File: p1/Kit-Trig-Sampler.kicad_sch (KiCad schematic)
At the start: 78 parts, among them J1 START_CV, J10 AUDIO_INR, J11 AUDIO_OUTL, J12 Eurorack_Power_16pin_Unshroud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, J2 LENGTH_CV, J3 SAMP_CV, J4 PITCH CV, J5 REV_TRIG, J6 PLAY_TRIG, J7 END_OUT, J8 AUDIO_INL, J9 AUIDO_OUTR, U1 TL082_TH, U2 TL082_TH

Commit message: Small changes to pin assignments
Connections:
- net A1: now also C1.1, POT_PITCH1.2 (Center); no longer R3.2, R6.2
- net A3: now also C10.1, POT_START1.2 (Center); no longer R4.2, R7.2
- net A4: no longer C1.1, POT_PITCH1.2 (Center)
- net A5: now also R3.2, R6.2; no longer C2.1, POT_SAMP1.2 (Center)
- net A6: now also C18.1, R27.2; no longer C10.1, POT_START1.2 (Center)
- net A8: now also R4.2, R7.2
- net A9: now also C2.1, POT_SAMP1.2 (Center); no longer C18.1, R27.2
- net D10: no longer R20.1
- net D11: now also R18.1; no longer R24.2
- net D12: now also R19.1; no longer R21.1
- net D15: now also R12.1; no longer J5.1 (SIG)
- net D16: now also R32.2, SD1.8 (DAT1); no longer R31.2, SD1.7 (DAT0)
- net D17: now also R31.2, SD1.7 (DAT0); no longer R32.2, SD1.8 (DAT1)
- net D18: now also R30.2, SD1.3 (CMD); no longer R28.2, SD1.1 (DAT2)
- net D19: now also R28.2, SD1.1 (DAT2); no longer R30.2, SD1.3 (CMD)
- net D2: now also J5.1 (SIG); no longer R12.1
- net D3: now also R24.2; no longer R19.1
- net D5: now also R20.1
- net D7: now also R21.1; no longer R18.1
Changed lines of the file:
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@@
     (effects (font (size 1.27 1.27)) (justify left bottom))
   )
-  (text "Length_CV" (at 471.17 262.255 0)
-    (effects (font (size 1.27 1.27)) (justify left bottom))
-  )
-  (text "Rev_Trig" (at 387.985 267.335 0)
+  (text "Length_CV" (at 471.17 267.335 0)
+    (effects (font (size 1.27 1.27)) (justify left bottom))
+  )
+  (text "Rev_Trig" (at 387.985 272.415 0)
     (effects (font (size 1.27 1.27)) (justify left bottom))
   )
@@
     (effects (font (size 5.08 5.08) (thickness 1.016) bold italic) (justify left bottom))
   )
-  (text "Play_But_R" (at 327.66 272.415 0)
-    (effects (font (size 1.27 1.27)) (justify left bottom))
-  )
-  (text "Rev_But_G" (at 313.69 133.985 0)
+  (text "Play_But_R" (at 387.985 234.315 0)
+    (effects (font (size 1.27 1.27)) (justify left bottom))
+  )
+  (text "Rev_But_G" (at 366.395 143.51 0)
     (effects (font (size 1.27 1.27)) (justify left bottom))
   )
@@
     (effects (font (size 1.27 1.27)) (justify left bottom))
   )
-  (text "Start_Pot" (at 433.705 269.875 0)
+  (text "Start_Pot" (at 471.17 264.795 0)
     (effects (font (size 1.27 1.27)) (justify left bottom))
   )
@@
     (effects (font (size 1.27 1.27)) (justify left bottom))
   )
-  (text "SDMMC_D2" (at 497.84 88.9 180)
-    (effects (font (size 1.27 1.27)) (justify right bottom))
-  )
-  (text "SDMMC_D0" (at 497.84 73.66 180)
-    (effects (font (size 1.27 1.27)) (justify right bottom))
-  )
-  (text "Length_Pot" (at 471.17 269.875 0)
+  (text "SDMMC_D2" (at 497.84 83.82 180)
+    (effects (font (size 1.27 1.27)) (justify right bottom))
+  )
+  (text "SDMMC_D0" (at 497.84 71.12 180)
+    (effects (font (size 1.27 1.27)) (justify right bottom))
+  )
+  (text "Length_Pot" (at 471.805 269.875 0)
     (effects (font (size 1.27 1.27)) (justify left bottom))
   )
@@
     (effects (font (size 5.08 5.08) (thickness 1.016) bold italic) (justify left bottom))
   )
-  (text "Rev_But" (at 471.17 272.415 0)
+  (text "Rev_But" (at 434.34 269.875 0)
     (effects (font (size 1.27 1.27)) (justify left bottom))
   )
@@
     (effects (font (size 1.27 1.27)) (justify left bottom))
   )
-  (text "SDMMC_D1" (at 497.84 71.12 180)
+  (text "SDMMC_D1" (at 497.84 73.66 180)
     (effects (font (size 1.27 1.27)) (justify right bottom))
   )
@@
     (effects (font (size 5.08 5.08) (thickness 1.016) bold italic) (justify left bottom))
   )
-  (text "Pitch_Pot" (at 433.07 267.335 0)
-    (effects (font (size 1.27 1.27)) (justify left bottom))
-  )
-  (text "Bank_But_G" (at 416.56 230.505 0)
-    (effects (font (size 1.27 1.27)) (justify left bottom))
-  )
-  (text "Sample_Pot" (at 471.17 267.335 0)
+  (text "Pitch_Pot" (at 471.17 262.255 0)
+    (effects (font (size 1.27 1.27)) (justify left bottom))
+  )
+  (text "Bank_But_G" (at 328.295 272.415 0)
+    (effects (font (size 1.27 1.27)) (justify left bottom))
+  )
+  (text "Sample_Pot" (at 471.17 272.415 0)
     (effects (font (size 1.27 1.27)) (justify left bottom))
   )
@@
     (effects (font (size 1.27 1.27)) (justify left bottom))
   )
-  (text "Rev_But_G" (at 387.985 231.775 0)
+  (text "Rev_But_G" (at 387.35 231.775 0)
     (effects (font (size 1.27 1.27)) (justify left bottom))
   )
@@
     (effects (font (size 1.27 1.27)) (justify right bottom))
   )
-  (text "Play_But_G" (at 484.505 234.95 0)
+  (text "Play_But_G" (at 332.105 231.775 0)
     (effects (font (size 1.27 1.27)) (justify left bottom))
   )
@@
     (effects (font (size 1.27 1.27)) (justify right bottom))
   )
-  (text "Rev_But_R" (at 388.62 234.315 0)
+  (text "Rev_But_R" (at 484.505 235.585 0)
     (effects (font (size 1.27 1.27)) (justify left bottom))
   )
@@
     (effects (font (size 1.27 1.27)) (justify left bottom))
   )
-  (text "End_Out" (at 396.24 272.415 180)
+  (text "End_Out" (at 395.605 267.335 180)
     (effects (font (size 1.27 1.27)) (justify right bottom))
   )
@@
     (effects (font (size 1.27 1.27)) (justify left bottom))
   )
-  (text "SDMMC_D3" (at 497.84 83.82 180)
+  (text "SDMMC_D3" (at 497.84 88.9 180)
     (effects (font (size 1.27 1.27)) (justify right bottom))
   )
@@
     (effects (font (size 1.27 1.27)) (justify right bottom))
   )
-  (text "Rev_But_B" (at 367.665 144.145 0)
-    (effects (font (size 1.27 1.27)) (justify left bottom))
-  )
-  (text "Rev_But_B" (at 340.995 231.14 180)
+  (text "Rev_But_B" (at 311.785 133.35 0)
+    (effects (font (size 1.27 1.27)) (justify left bottom))
+  )
+  (text "Rev_But_B" (at 427.99 230.505 180)
     (effects (font (size 1.27 1.27)) (justify right bottom))
   )
@@
     (effects (font (size 1.27 1.27)) (justify left bottom))
   )
-  (text "Sample_CV" (at 471.17 264.795 0)
+  (text "Sample_CV" (at 431.165 272.415 0)
     (effects (font (size 1.27 1.27)) (justify left bottom))
   )
@@
     (effects (font (size 1.27 1.27)) (justify left bottom))
   )
-  (label "D7" (at 321.945 100.33 0)
+  (label "D11" (at 321.945 100.33 0)
     (effects (font (size 1.27 1.27)) (justify left bottom))
   )
@@
     (effects (font (size 1.27 1.27)) (justify right bottom))
   )
-  (label "A4" (at 52.07 239.395 180)
+  (label "A1" (at 52.07 239.395 180)
     (effects (font (size 1.27 1.27)) (justify right bottom))
   )
@@
     (effects (font (size 1.27 1.27)) (justify left bottom))
   )
-  (label "D11" (at 372.745 140.97 180)
+  (label "D3" (at 372.745 140.97 180)
     (effects (font (size 1.27 1.27)) (justify right bottom))
   )
@@
     (effects (font (size 1.27 1.27)) (justify right bottom))
   )
-  (label "D2" (at 152.4 115.57 0)
+  (label "D15" (at 152.4 115.57 0)
     (effects (font (size 1.27 1.27)) (justify left bottom))
   )
@@
     (effects (font (size 1.27 1.27)) (justify right bottom))
   )
-  (label "D18" (at 482.6 88.9 0)
-    (effects (font (size 1.27 1.27)) (justify left bottom))
-  )
-  (label "D16" (at 482.6 73.66 0)
+  (label "D18" (at 482.6 83.82 0)
+    (effects (font (size 1.27 1.27)) (justify left bottom))
+  )
+  (label "D16" (at 482.6 71.12 0)
     (effects (font (size 1.27 1.27)) (justify left bottom))
   )
@@
     (effects (font (size 1.27 1.27)) (justify right bottom))
   )
-  (label "A6" (at 111.125 271.78 180)
+  (label "A3" (at 111.125 271.78 180)
     (effects (font (size 1.27 1.27)) (justify right bottom))
   )
@@
     (effects (font (size 1.27 1.27)) (justify right bottom))
   )
-  (label "A5" (at 52.705 271.78 180)
-    (effects (font (size 1.27 1.27)) (justify right bottom))
-  )
-  (label "D15" (at 171.45 49.53 180)
+  (label "A9" (at 52.705 271.78 180)
+    (effects (font (size 1.27 1.27)) (justify right bottom))
+  )
+  (label "D2" (at 171.45 49.53 180)
     (effects (font (size 1.27 1.27)) (justify right bottom))
   )
@@
     (effects (font (size 1.27 1.27)) (justify right bottom))
   )
-  (label "D19" (at 482.6 83.82 0)
-    (effects (font (size 1.27 1.27)) (justify left bottom))
-  )
-  (label "A9" (at 374.015 125.73 180)
+  (label "D19" (at 482.6 88.9 0)
+    (effects (font (size 1.27 1.27)) (justify left bottom))
+  )
+  (label "A6" (at 374.015 125.73 180)
     (effects (font (size 1.27 1.27)) (justify right bottom))
   )
@@
     (effects (font (size 1.27 1.27)) (justify left bottom))
   )
-  (label "D12" (at 321.945 140.97 0)
+  (label "D7" (at 321.945 140.97 0)
     (effects (font (size 1.27 1.27)) (justify left bottom))
   )
@@
     (effects (font (size 1.27 1.27)) (justify right bottom))
   )
-  (label "A3" (at 73.025 127.635 180)
-    (effects (font (size 1.27 1.27)) (justify right bottom))
-  )
-  (label "D3" (at 321.945 105.41 0)
+  (label "A8" (at 73.025 127.635 180)
+    (effects (font (size 1.27 1.27)) (justify right bottom))
+  )
+  (label "D12" (at 321.945 105.41 0)
     (effects (font (size 1.27 1.27)) (justify left bottom))
   )
@@
     (effects (font (size 1.27 1.27)) (justify right bottom))
   )
-  (label "D17" (at 482.6 71.12 0)
+  (label "D17" (at 482.6 73.66 0)
     (effects (font (size 1.27 1.27)) (justify left bottom))
   )
@@
     (effects (font (size 1.27 1.27)) (justify left bottom))
   )
-  (label "D10" (at 321.945 135.89 0)
-    (effects (font (size 1.27 1.27)) (justify left bottom))
-  )
-  (label "A1" (at 72.39 86.36 180)
-    (effects (font (size 1.27 1.27)) (justify right bottom))
-  )
+  (label "D5" (at 321.945 135.89 0)
+    (effects (font (size 1.27 1.27)) (justify left bottom))
+  )
+  (label "A5" (at 72.39 86.36 180)
+    (effects (font (size 1.27 1.27)) (justify right bottom))
+  )

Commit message: added Bank cv
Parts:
- added J13: BANK_CV, 4ms_Jack:EighthInch_PJ398SM, symbol 4ms_Jack:3.5mm_Mono_Switched
- added R33: 47k_TH0.125, 4ms_Resistor:R_Axial_DIN0207_L6.3mm_D2.5mm_P7.62mm_Horizontal, symbol 4ms_Resistor_TH:47k_TH0.125
- added R34: 100k_TH0.125, 4ms_Resistor:R_Axial_DIN0207_L6.3mm_D2.5mm_P7.62mm_Horizontal, symbol 4ms_Resistor_TH:100k_TH0.125
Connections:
- net A4: now also R33.2, R34.2
- net GND: now also J13.2 (SHEILD), J13.3 (SW), R34.1
- new net: J13.1 (SIG), R33.1
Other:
- note added: "BANK_CV"
- moved on the sheet: C1, C10, C2, C3, C6, C9, J10, J11, J4, J8, J9, POT_LENGTH1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

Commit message: part placement ip
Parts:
- renumbered J12 to J14
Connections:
- net D10: now also R24.2
- net D3: no longer R24.2
- net at C11.2, R14.2, R15.1: now also U2.1; no longer U2.7
- net at C11.1, R13.2, R14.1: now also U2.2 (-); no longer U2.6 (-)
- net at R12.2: now also U2.3 (+); no longer U2.5 (+)
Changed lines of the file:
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@@
     (effects (font (size 1.27 1.27)) (justify left bottom))
   )
-  (label "D3" (at 372.745 140.97 180)
+  (label "D10" (at 372.745 140.97 180)
     (effects (font (size 1.27 1.27)) (justify right bottom))
   )
@@
   (symbol (lib_id "4ms_Connector:Eurorack_Power_16pin_Unshrouded") (at 38.735 369.57 0) (unit 1)
     (in_bom yes) (on_board yes) (fields_autoplaced)
-    (property "Reference" "J12" (id 0) (at 36.6363 383.54 0))
+    (property "Reference" "J14" (id 0) (at 36.6363 383.54 0))
     (property "Value" "Eurorack_Power_16pin_Unshrouded" (id 1) (at 36.6363 386.08 0))
     (property "Footprint" "4ms_Connector:Pins_2x08_2.54mm_TH_EuroPower" (id 2) (at 48.895 392.43 0)
@@
     (pin "1")
   )
-  (symbol (lib_id "4ms_IC:TL082_TH") (at 191.77 118.11 0) (unit 2)
+  (symbol (lib_id "4ms_IC:TL082_TH") (at 191.77 118.11 0) (unit 1)
     (in_bom yes) (on_board yes) (fields_autoplaced)
     (property "Reference" "U2" (id 0) (at 191.77 107.95 0))
@@
       (reference "J11") (unit 1) (value "AUDIO_OUTL") (footprint "4ms_Jack:EighthInch_PJ398SM")
     )
-    (path "/26de500a-6a5a-4f52-a622-63f695723fe5"
-      (reference "J12") (unit 1) (value "Eurorack_Power_16pin_Unshrouded") (footprint "4ms_Connector:Pins_2x08_2.54mm_TH_EuroPower")
-    )
     (path "/8dfd5b71-d7ca-434d-99e0-1511a2784fa0"
       (reference "J13") (unit 1) (value "BANK_CV") (footprint "4ms_Jack:EighthInch_PJ398SM")
     )
+    (path "/26de500a-6a5a-4f52-a622-63f695723fe5"
+      (reference "J14") (unit 1) (value "Eurorack_Power_16pin_Unshrouded") (footprint "4ms_Connector:Pins_2x08_2.54mm_TH_EuroPower")
+    )
     (path "/aa429c81-7bec-4d11-98d8-90f9522e0b59"
       (reference "JA1") (unit 1) (value "Socket_02x05_TH") (footprint "4ms_Connector:Socket_2x05_2.54mm_TH")
@@
     )
     (path "/e9d45a74-69c4-44b2-aeb2-b4cba2a5826a"
-      (reference "U2") (unit 2) (value "TL082_TH") (footprint "4ms_Package_DIP:DIP-8pin_TH")
+      (reference "U2") (unit 1) (value "TL082_TH") (footprint "4ms_Package_DIP:DIP-8pin_TH")
     )
     (path "/867c8e1f-3163-4dae-bd9c-3cfb52f58b42"

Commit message: small updates
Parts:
- Bank_But1: renamed from BANK_BUT1; footprint 4ms_Switch:Button_RgbLED_SPST_PB615303HL-7mm -> 4ms_Switch:Button_RgbLED_SPST_TC002
- REV_BUT1: footprint 4ms_Switch:Button_RgbLED_SPST_PB615303HL-7mm -> 4ms_Switch:Button_RgbLED_SPST_TC002
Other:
- moved on the sheet: J10, J8, J9

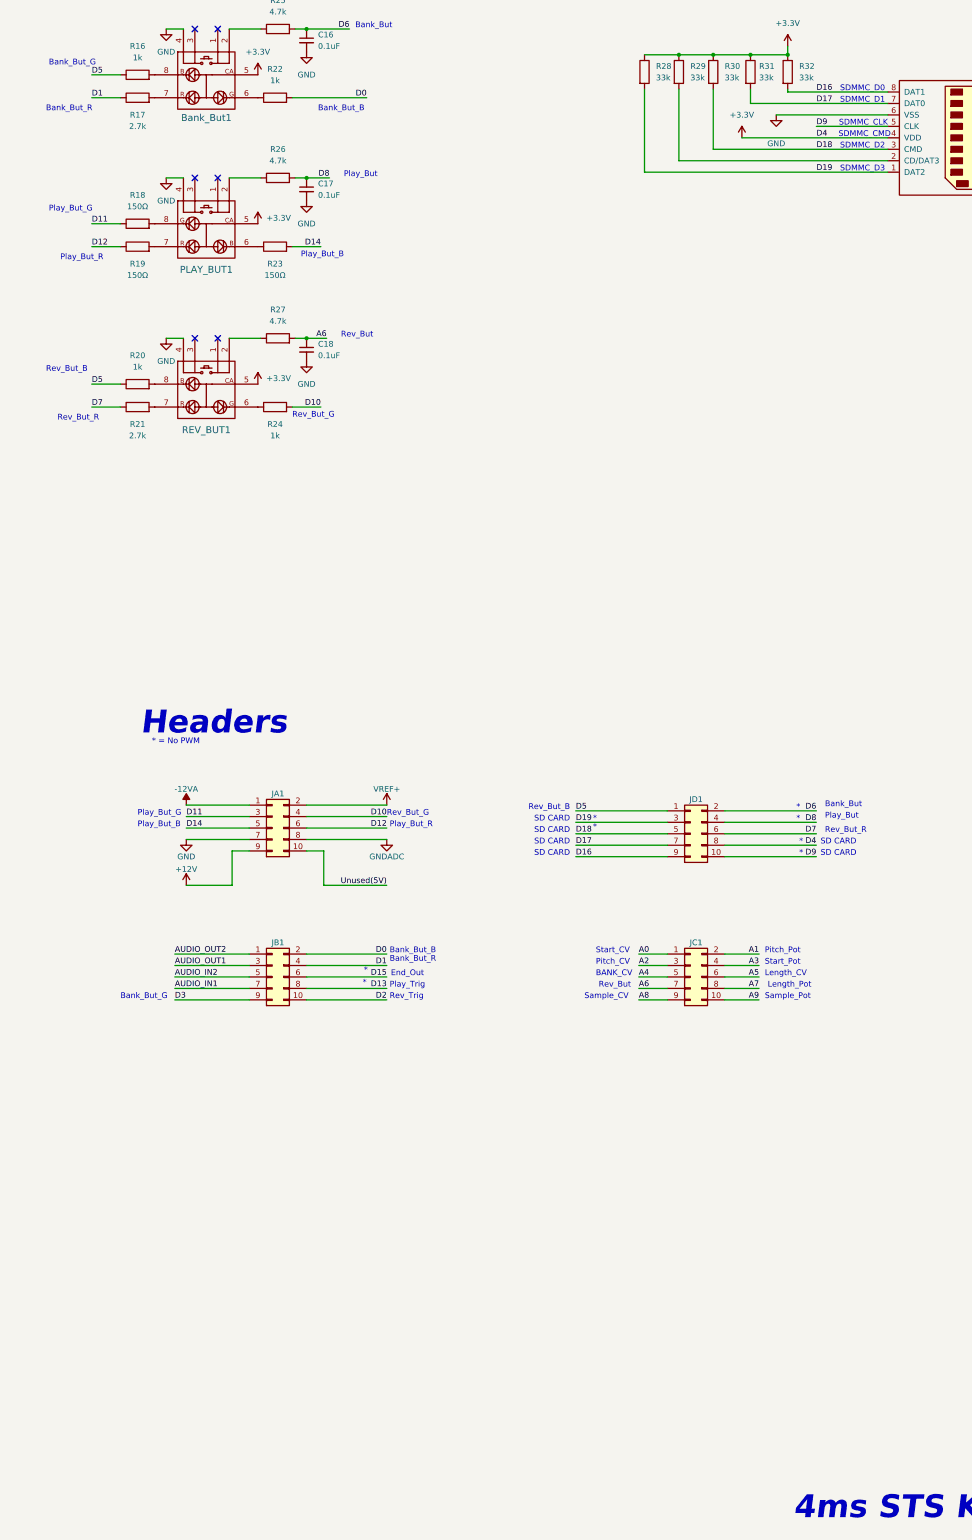
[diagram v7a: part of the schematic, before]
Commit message: nudged some parts in accordance to FP update
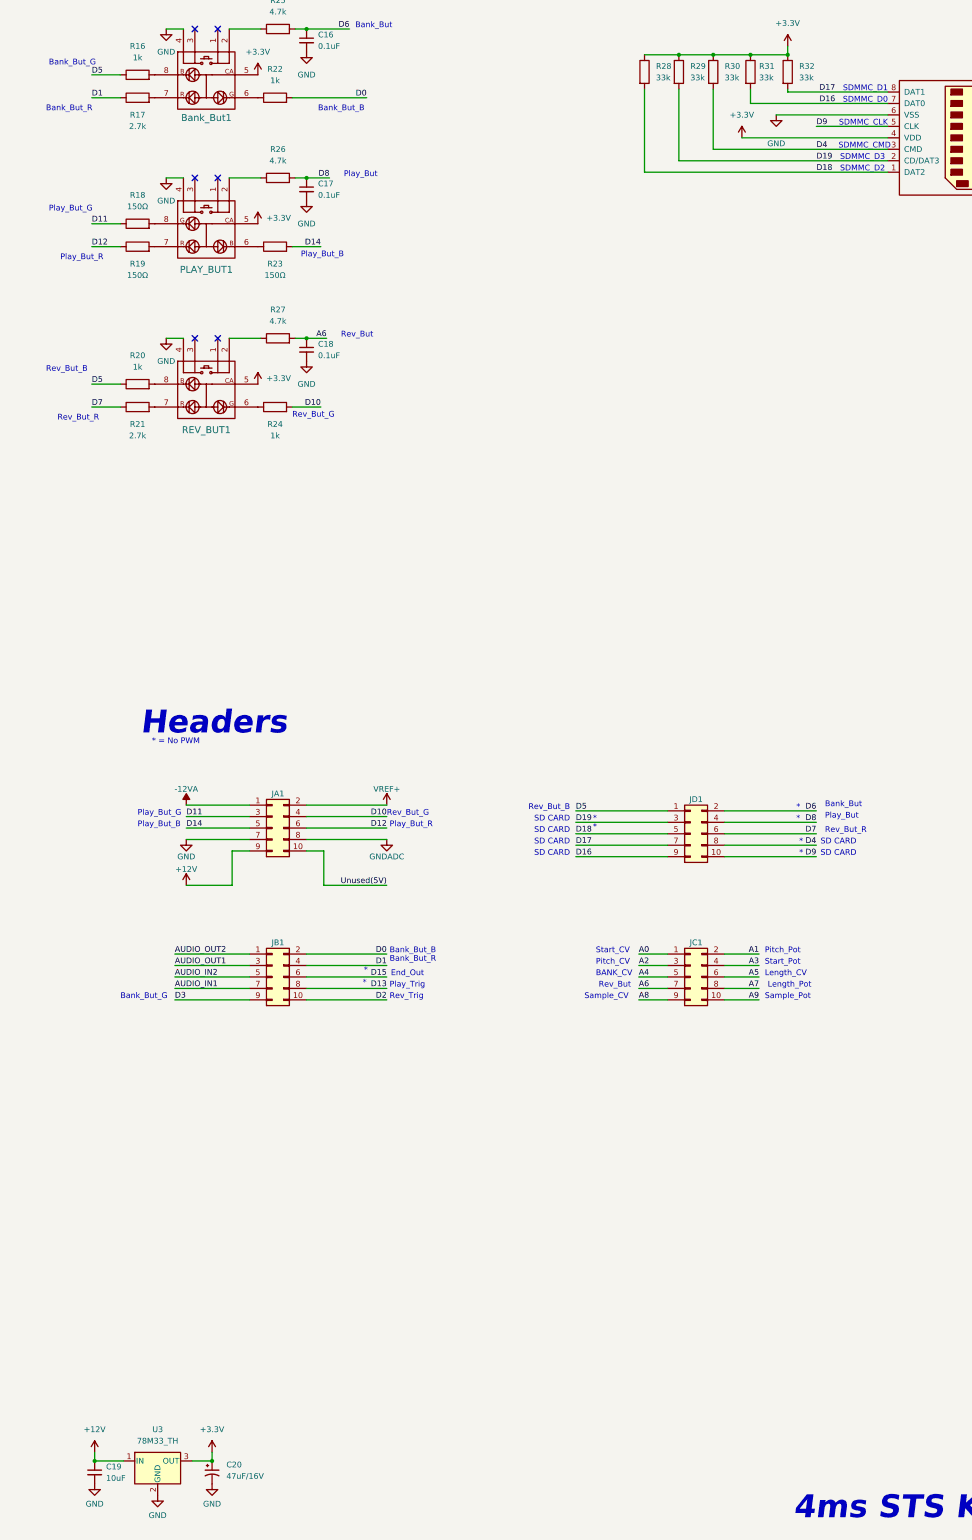
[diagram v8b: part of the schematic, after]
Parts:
- added C19: 10uF_Radial_TH, 4ms_Capacitor:CP_Radial_P2.5mm, symbol 4ms_Capacitor:10uF_Radial_TH
- added C20: 47uF_16V_TH, 4ms_Capacitor:CP_Radial_P2.5mm, symbol 4ms_Capacitor:47uF_16V_TH
- added U3: 78M33_TH, Package_TO_SOT_THT:TO-220-3_Vertical, symbol 4ms_Regulator:78M33_TH
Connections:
- net +12V: now also C19.1, U3.1 (IN)
- net +3V3: now also C20.1, U3.3 (OUT); no longer JD1.8 (GND)
- net D16: now also R31.2, SD1.7 (DAT0); no longer R32.2, SD1.8 (DAT1)
- net D17: now also R32.2, SD1.8 (DAT1); no longer R31.2, SD1.7 (DAT0)
- net D18: now also R28.2, SD1.1 (DAT2); no longer R30.2, SD1.3 (CMD)
- net D19: now also R29.2, SD1.2 (CD/DAT3); no longer R28.2, SD1.1 (DAT2)
- net GND: now also C19.2, C20.2, U3.2 (GND)
- new net D4: JD1.8 (GND), R30.2, SD1.3 (CMD)
